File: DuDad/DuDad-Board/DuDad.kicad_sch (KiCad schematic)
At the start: 24 parts, among them J1 EXP, J2 USB_B_Micro, J3 USB_A, Q1 2N3906, Q2 2N3906, Q3 2N7000, Q4 2N3906, SW1 Reset

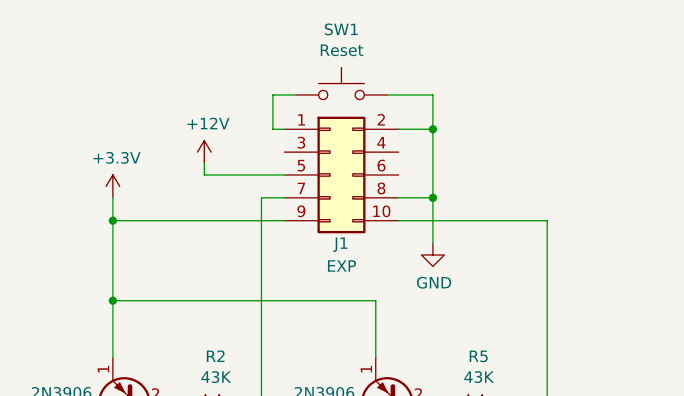
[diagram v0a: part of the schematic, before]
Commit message: Updates readme and DuDad board.
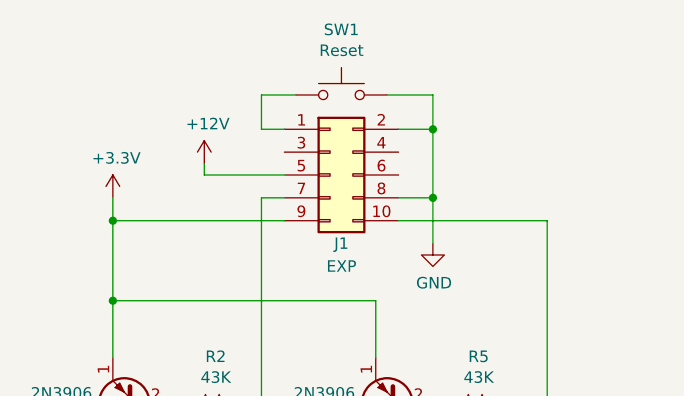
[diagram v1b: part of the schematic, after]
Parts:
- D1: Digi-Key Part 160-1035-ND -> 732-5005-ND
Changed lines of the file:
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@@
     (stroke (width 0) (type default) (color 0 0 0 0))
   )
-  (wire (pts (xy 49.53 33.02) (xy 49.53 29.21))
+  (wire (pts (xy 48.26 33.02) (xy 48.26 29.21))
     (stroke (width 0) (type default) (color 0 0 0 0))
   )
@@
     (stroke (width 0) (type default) (color 0 0 0 0))
   )
-  (wire (pts (xy 49.53 29.21) (xy 52.07 29.21))
+  (wire (pts (xy 48.26 29.21) (xy 52.07 29.21))
     (stroke (width 0) (type default) (color 0 0 0 0))
   )
@@
     (stroke (width 0) (type default) (color 0 0 0 0))
   )
-  (wire (pts (xy 50.8 33.02) (xy 49.53 33.02))
+  (wire (pts (xy 50.8 33.02) (xy 48.26 33.02))
     (stroke (width 0) (type default) (color 0 0 0 0))
   )
@@
       (effects (font (size 1.27 1.27)) hide)
     )
-    (property "Digi-Key Part" "160-1035-ND" (id 4) (at 31.75 73.66 90)
-      (effects (font (size 1.27 1.27)) hide)
-    )
+    (property "Digi-Key Part" "732-5005-ND" (id 4) (at 31.75 73.66 90)
+      (effects (font (size 1.27 1.27)) hide)
+    )

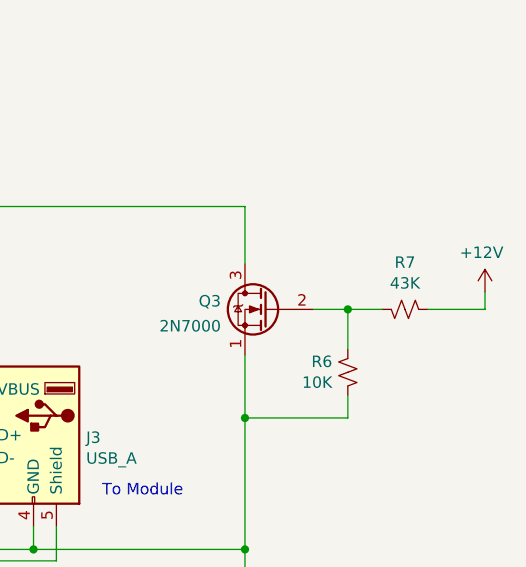
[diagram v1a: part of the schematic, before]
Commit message: Updates readme, moves docs to docs folder
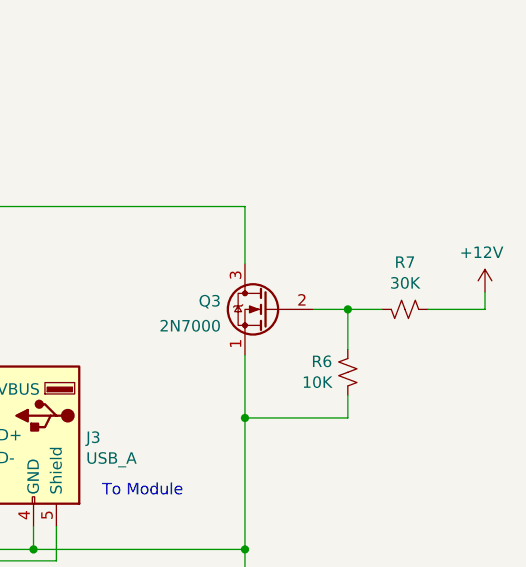
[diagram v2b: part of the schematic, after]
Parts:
- R7: value 43K -> 30K; Digi-Key Part CF14JT43K0CT-ND -> CF14JT30K0CT-ND
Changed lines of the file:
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@@
     (in_bom yes) (on_board yes)
     (property "Reference" "R7" (id 0) (at 187.96 69.088 90))
-    (property "Value" "43K" (id 1) (at 187.96 71.3994 90))
+    (property "Value" "30K" (id 1) (at 187.96 71.3994 90))
     (property "Footprint" "Resistor_THT:R_Axial_DIN0207_L6.3mm_D2.5mm_P10.16mm_Horizontal" (id 2) (at 187.96 74.295 0)
       (effects (font (size 1.27 1.27)) hide)
@@
       (effects (font (size 1.27 1.27)) hide)
     )
-    (property "Digi-Key Part" "CF14JT43K0CT-ND" (id 4) (at 187.96 74.295 90)
+    (property "Digi-Key Part" "CF14JT30K0CT-ND" (id 4) (at 187.96 74.295 90)
       (effects (font (size 1.27 1.27)) hide)
     )
@@
     )
     (path "/455ab60b-7725-47c1-8bea-8bb2de9c3df5"
-      (reference "R7") (unit 1) (value "43K") (footprint "Resistor_THT:R_Axial_DIN0207_L6.3mm_D2.5mm_P10.16mm_Horizontal")
+      (reference "R7") (unit 1) (value "30K") (footprint "Resistor_THT:R_Axial_DIN0207_L6.3mm_D2.5mm_P10.16mm_Horizontal")
     )
     (path "/cb20dedd-c678-4d7e-b310-0959ee8ccdca"

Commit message: Adds 2HP DuDad
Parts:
- J1:   LCSC Part # (none) -> C225520
- J3:   LCSC Part # (none) -> C718031
- Q1, Q2, Q4:   LCSC Part # (none) -> C9809
- Q3:   LCSC Part # (none) -> C232838
- R1, R4:   LCSC Part # (none) -> C119309
- R2, R5, R8:   LCSC Part # (none) -> C433719
- R3:   LCSC Part # (none) -> C410696
- R6, R9:   LCSC Part # (none) -> C433778
- R7:   LCSC Part # (none) -> C176499
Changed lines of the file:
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@@
+      (effects (font (size 1.27 1.27)) hide)
+    )
+    (property "  LCSC Part #" "C9809" (id 5) (at 63.5 63.5 0)
       (effects (font (size 1.27 1.27)) hide)
     )
@@
       (effects (font (size 1.27 1.27)) hide)
     )
+    (property "  LCSC Part #" "C433719" (id 5) (at 72.39 63.5 0)
+      (effects (font (size 1.27 1.27)) hide)
+    )
     (pin "1")
     (pin "2")
@@
     )
     (property "Digi-Key Part" "CF14JT200RCT-ND" (id 4) (at 60.96 81.28 0)
+      (effects (font (size 1.27 1.27)) hide)
+    )
+    (property "  LCSC Part #" "C119309" (id 5) (at 60.96 81.28 0)
       (effects (font (size 1.27 1.27)) hide)
     )
@@
       (effects (font (size 1.27 1.27)) hide)
     )
+    (property "  LCSC Part #" "C9809" (id 5) (at 34.29 63.5 0)
+      (effects (font (size 1.27 1.27)) hide)
+    )
     (pin "1")
     (pin "2")
@@
       (effects (font (size 1.27 1.27)) hide)
     )
+    (property "  LCSC Part #" "C433719" (id 5) (at 43.18 63.5 0)
+      (effects (font (size 1.27 1.27)) hide)
+    )
     (pin "1")
     (pin "2")
@@
     )
     (property "Digi-Key Part" "CF14JT200RCT-ND" (id 4) (at 31.75 81.28 0)
+      (effects (font (size 1.27 1.27)) hide)
+    )
+    (property "  LCSC Part #" "C119309" (id 5) (at 31.75 81.28 0)
       (effects (font (size 1.27 1.27)) hide)
     )
@@
     )
     (property "Digi-Key Part" "738-CFF14JT1K00CT-ND" (id 4) (at 133.985 120.015 0)
+      (effects (font (size 1.27 1.27)) hide)
+    )
+    (property "  LCSC Part #" "C410696" (id 5) (at 133.985 120.015 0)
       (effects (font (size 1.27 1.27)) hide)
     )
@@
       (effects (font (size 1.27 1.27)) hide)
     )
+    (property "  LCSC Part #" "C718031" (id 5) (at 146.685 88.265 0)
+      (effects (font (size 1.27 1.27)) hide)
+    )
     (pin "1")
     (pin "2")
@@
     )
     (property "Digi-Key Part" "S2011EC-05-ND" (id 4) (at 55.88 38.1 0)
+      (effects (font (size 1.27 1.27)) hide)
+    )
+    (property "  LCSC Part #" "C225520" (id 5) (at 55.88 38.1 0)
       (effects (font (size 1.27 1.27)) hide)
     )
@@
       (effects (font (size 1.27 1.27)) hide)
     )
+    (property "  LCSC Part #" "C9809" (id 5) (at 120.65 80.645 0)
+      (effects (font (size 1.27 1.27)) hide)
+    )
     (pin "1")
     (pin "2")
@@
       (effects (font (size 1.27 1.27)) hide)
     )
+    (property "  LCSC Part #" "C176499" (id 5) (at 187.96 74.295 90)
+      (effects (font (size 1.27 1.27)) hide)
+    )
     (pin "1")
     (pin "2")
@@
     )
     (property "Digi-Key Part" "CF14JT10K0CT-ND" (id 4) (at 131.445 62.865 0)
+      (effects (font (size 1.27 1.27)) hide)
+    )
+    (property "  LCSC Part #" "C433778" (id 5) (at 131.445 62.865 0)
       (effects (font (size 1.27 1.27)) hide)
     )
@@
       (effects (font (size 1.27 1.27)) hide)
     )
+    (property "  LCSC Part #" "C232838" (id 5) (at 172.72 74.295 0)
+      (effects (font (size 1.27 1.27)) hide)
+    )
     (pin "1")
     (pin "2")
@@
       (effects (font (size 1.27 1.27)) hide)
     )
+    (property "  LCSC Part #" "C433719" (id 5) (at 112.395 72.39 0)
+      (effects (font (size 1.27 1.27)) hide)
+    )
     (pin "1")
     (pin "2")
@@
       (effects (font (size 1.27 1.27)) hide)
     )
+    (property "  LCSC Part #" "C433778" (id 5) (at 181.61 81.28 0)
+      (effects (font (size 1.27 1.27)) hide)
+    )

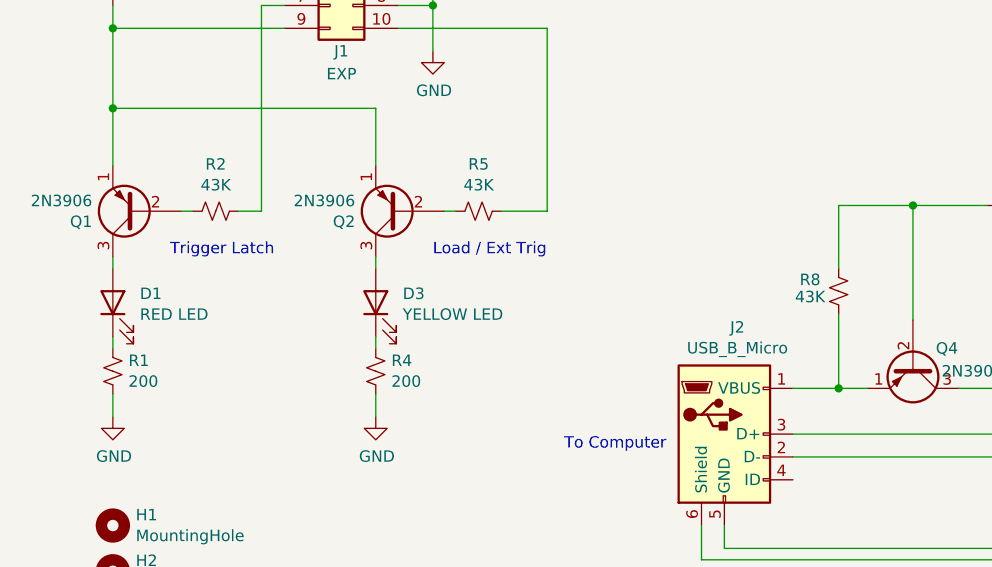
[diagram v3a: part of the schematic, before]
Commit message: Ups resistor values to dim LEDs. Adds generate BOMs.
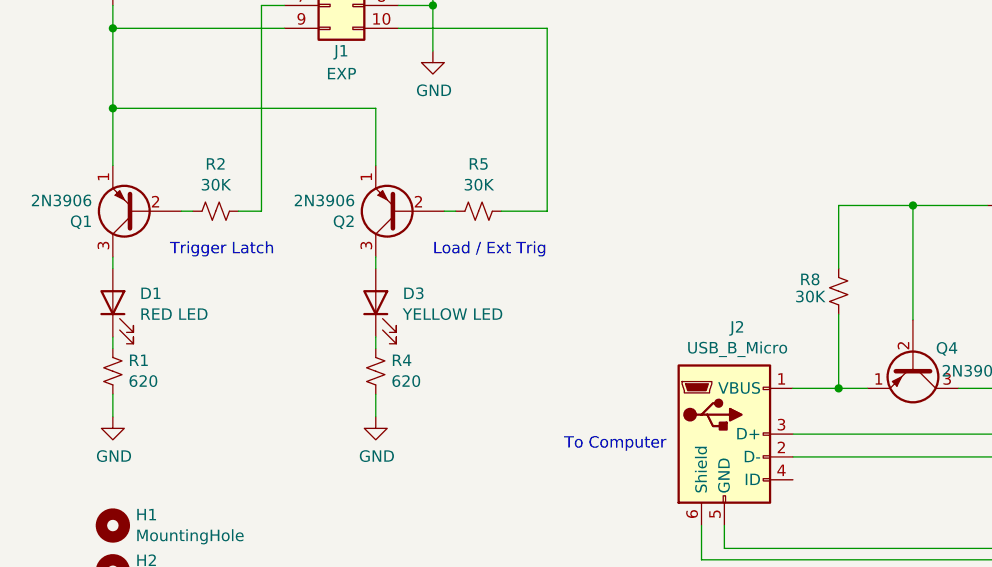
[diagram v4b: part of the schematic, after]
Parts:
- J1:   LCSC Part # C225520 -> (none); LCSC Part # (none) -> C225520
- J3:   LCSC Part # C718031 -> (none); LCSC Part # (none) -> C386737
- Q1, Q2, Q4:   LCSC Part # C9809 -> (none); LCSC Part # (none) -> C9809
- Q3:   LCSC Part # C232838 -> (none); LCSC Part # (none) -> C232838
- R1, R4: value 200 -> 620;   LCSC Part # C119309 -> (none); Digi-Key Part CF14JT200RCT-ND -> CF14JT620RCT-ND; LCSC Part # (none) -> C120050
- R2, R5, R8: value 43K -> 30K;   LCSC Part # C433719 -> (none); Digi-Key Part CF14JT43K0CT-ND -> CF14JT30K0CT-ND; LCSC Part # (none) -> C176499
- R3:   LCSC Part # C410696 -> (none); Digi-Key Part 738-CFF14JT1K00CT-ND -> CF14JT1K00CT-ND; LCSC Part # (none) -> C120055
- R6, R9:   LCSC Part # C433778 -> (none); LCSC Part # (none) -> C433778
- R7:   LCSC Part # C176499 -> (none); LCSC Part # (none) -> C176499
- SW1: Digi-Key Part 450-1940-ND -> 450-1653-ND
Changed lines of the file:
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@@
       (effects (font (size 1.27 1.27)) hide)
     )
-    (property "  LCSC Part #" "C9809" (id 5) (at 63.5 63.5 0)
+    (property "LCSC Part #" "C9809" (id 5) (at 63.5 63.5 0)
       (effects (font (size 1.27 1.27)) hide)
     )
@@
     (in_bom yes) (on_board yes)
     (property "Reference" "R5" (id 0) (at 72.39 58.293 90))
-    (property "Value" "43K" (id 1) (at 72.39 60.6044 90))
+    (property "Value" "30K" (id 1) (at 72.39 60.6044 90))
     (property "Footprint" "Resistor_THT:R_Axial_DIN0207_L6.3mm_D2.5mm_P10.16mm_Horizontal" (id 2) (at 72.39 63.5 0)
       (effects (font (size 1.27 1.27)) hide)
@@
       (effects (font (size 1.27 1.27)) hide)
     )
-    (property "Digi-Key Part" "CF14JT43K0CT-ND" (id 4) (at 72.39 63.5 90)
-      (effects (font (size 1.27 1.27)) hide)
-    )
-    (property "  LCSC Part #" "C433719" (id 5) (at 72.39 63.5 0)
+    (property "Digi-Key Part" "CF14JT30K0CT-ND" (id 4) (at 72.39 63.5 90)
+      (effects (font (size 1.27 1.27)) hide)
+    )
+    (property "LCSC Part #" "C176499" (id 5) (at 72.39 63.5 0)
       (effects (font (size 1.27 1.27)) hide)
     )
@@
       (effects (font (size 1.27 1.27)) (justify right))
     )
-    (property "Value" "200" (id 1) (at 62.6872 82.423 0)
+    (property "Value" "620" (id 1) (at 62.6872 82.423 0)
       (effects (font (size 1.27 1.27)) (justify right))
     )
@@
       (effects (font (size 1.27 1.27)) hide)
     )
-    (property "Digi-Key Part" "CF14JT200RCT-ND" (id 4) (at 60.96 81.28 0)
-      (effects (font (size 1.27 1.27)) hide)
-    )
-    (property "  LCSC Part #" "C119309" (id 5) (at 60.96 81.28 0)
+    (property "Digi-Key Part" "CF14JT620RCT-ND" (id 4) (at 60.96 81.28 0)
+      (effects (font (size 1.27 1.27)) hide)
+    )
+    (property "LCSC Part #" "C120050" (id 5) (at 60.96 81.28 0)
       (effects (font (size 1.27 1.27)) hide)
     )
@@
       (effects (font (size 1.27 1.27)) hide)
     )
-    (property "Digi-Key Part" "450-1940-ND" (id 4) (at 57.15 29.21 0)
+    (property "Digi-Key Part" "450-1653-ND" (id 4) (at 57.15 29.21 0)
       (effects (font (size 1.27 1.27)) hide)
     )
@@
       (effects (font (size 1.27 1.27)) hide)
     )
-    (property "  LCSC Part #" "C9809" (id 5) (at 34.29 63.5 0)
+    (property "LCSC Part #" "C9809" (id 5) (at 34.29 63.5 0)
       (effects (font (size 1.27 1.27)) hide)
     )
@@
     (in_bom yes) (on_board yes)
     (property "Reference" "R2" (id 0) (at 43.18 58.293 90))
-    (property "Value" "43K" (id 1) (at 43.18 60.6044 90))
+    (property "Value" "30K" (id 1) (at 43.18 60.6044 90))
     (property "Footprint" "Resistor_THT:R_Axial_DIN0207_L6.3mm_D2.5mm_P10.16mm_Horizontal" (id 2) (at 43.18 63.5 0)
       (effects (font (size 1.27 1.27)) hide)
@@
       (effects (font (size 1.27 1.27)) hide)
     )
-    (property "Digi-Key Part" "CF14JT43K0CT-ND" (id 4) (at 43.18 63.5 90)
-      (effects (font (size 1.27 1.27)) hide)
-    )
-    (property "  LCSC Part #" "C433719" (id 5) (at 43.18 63.5 0)
+    (property "Digi-Key Part" "CF14JT30K0CT-ND" (id 4) (at 43.18 63.5 90)
+      (effects (font (size 1.27 1.27)) hide)
+    )
+    (property "LCSC Part #" "C176499" (id 5) (at 43.18 63.5 0)
       (effects (font (size 1.27 1.27)) hide)
     )
@@
       (effects (font (size 1.27 1.27)) (justify right))
     )
-    (property "Value" "200" (id 1) (at 33.4772 82.423 0)
+    (property "Value" "620" (id 1) (at 33.4772 82.423 0)
       (effects (font (size 1.27 1.27)) (justify right))
     )
@@
       (effects (font (size 1.27 1.27)) hide)
     )
-    (property "Digi-Key Part" "CF14JT200RCT-ND" (id 4) (at 31.75 81.28 0)
-      (effects (font (size 1.27 1.27)) hide)
-    )
-    (property "  LCSC Part #" "C119309" (id 5) (at 31.75 81.28 0)
+    (property "Digi-Key Part" "CF14JT620RCT-ND" (id 4) (at 31.75 81.28 0)
+      (effects (font (size 1.27 1.27)) hide)
+    )
+    (property "LCSC Part #" "C120050" (id 5) (at 31.75 81.28 0)
       (effects (font (size 1.27 1.27)) hide)
     )
@@
       (effects (font (size 1.27 1.27)) hide)
     )
-    (property "Digi-Key Part" "738-CFF14JT1K00CT-ND" (id 4) (at 133.985 120.015 0)
-      (effects (font (size 1.27 1.27)) hide)
-    )
-    (property "  LCSC Part #" "C410696" (id 5) (at 133.985 120.015 0)
+    (property "Digi-Key Part" "CF14JT1K00CT-ND" (id 4) (at 133.985 120.015 0)
+      (effects (font (size 1.27 1.27)) hide)
+    )
+    (property "LCSC Part #" "C120055" (id 5) (at 133.985 120.015 0)
       (effects (font (size 1.27 1.27)) hide)
     )
@@
       (effects (font (size 1.27 1.27)) hide)
     )
-    (property "  LCSC Part #" "C718031" (id 5) (at 146.685 88.265 0)
+    (property "LCSC Part #" "C386737" (id 5) (at 146.685 88.265 0)
       (effects (font (size 1.27 1.27)) hide)
     )
@@
       (effects (font (size 1.27 1.27)) hide)
     )
-    (property "  LCSC Part #" "C225520" (id 5) (at 55.88 38.1 0)
+    (property "LCSC Part #" "C225520" (id 5) (at 55.88 38.1 0)
       (effects (font (size 1.27 1.27)) hide)
     )
@@
       (effects (font (size 1.27 1.27)) hide)
     )
-    (property "  LCSC Part #" "C9809" (id 5) (at 120.65 80.645 0)
+    (property "LCSC Part #" "C9809" (id 5) (at 120.65 80.645 0)
       (effects (font (size 1.27 1.27)) hide)
     )
@@
       (effects (font (size 1.27 1.27)) hide)
     )
-    (property "  LCSC Part #" "C176499" (id 5) (at 187.96 74.295 90)
+    (property "LCSC Part #" "C176499" (id 5) (at 187.96 74.295 90)
       (effects (font (size 1.27 1.27)) hide)
     )
@@
       (effects (font (size 1.27 1.27)) hide)
     )
-    (property "  LCSC Part #" "C433778" (id 5) (at 131.445 62.865 0)
+    (property "LCSC Part #" "C433778" (id 5) (at 131.445 62.865 0)
       (effects (font (size 1.27 1.27)) hide)
     )
@@
       (effects (font (size 1.27 1.27)) hide)
     )
-    (property "  LCSC Part #" "C232838" (id 5) (at 172.72 74.295 0)
+    (property "LCSC Part #" "C232838" (id 5) (at 172.72 74.295 0)
       (effects (font (size 1.27 1.27)) hide)
     )
@@
     (in_bom yes) (on_board yes)
     (property "Reference" "R8" (id 0) (at 109.22 71.12 0))
-    (property "Value" "43K" (id 1) (at 109.22 73.025 0))
+    (property "Value" "30K" (id 1) (at 109.22 73.025 0))
     (property "Footprint" "Resistor_THT:R_Axial_DIN0207_L6.3mm_D2.5mm_P10.16mm_Horizontal" (id 2) (at 112.395 72.39 0)
       (effects (font (size 1.27 1.27)) hide)
@@
       (effects (font (size 1.27 1.27)) hide)
     )
-    (property "Digi-Key Part" "CF14JT43K0CT-ND" (id 4) (at 112.395 72.39 90)
-      (effects (font (size 1.27 1.27)) hide)
-    )
-    (property "  LCSC Part #" "C433719" (id 5) (at 112.395 72.39 0)
+    (property "Digi-Key Part" "CF14JT30K0CT-ND" (id 4) (at 112.395 72.39 90)
+      (effects (font (size 1.27 1.27)) hide)
+    )
+    (property "LCSC Part #" "C176499" (id 5) (at 112.395 72.39 0)
       (effects (font (size 1.27 1.27)) hide)
     )
@@
       (effects (font (size 1.27 1.27)) hide)
     )
-    (property "  LCSC Part #" "C433778" (id 5) (at 181.61 81.28 0)
+    (property "LCSC Part #" "C433778" (id 5) (at 181.61 81.28 0)
       (effects (font (size 1.27 1.27)) hide)
     )
@@
     )
     (path "/00000000-0000-0000-0000-0000620129e0"
-      (reference "R1") (unit 1) (value "200") (footprint "Resistor_THT:R_Axial_DIN0207_L6.3mm_D2.5mm_P10.16mm_Horizontal")
+      (reference "R1") (unit 1) (value "620") (footprint "Resistor_THT:R_Axial_DIN0207_L6.3mm_D2.5mm_P10.16mm_Horizontal")
     )
     (path "/00000000-0000-0000-0000-000062010975"
-      (reference "R2") (unit 1) (value "43K") (footprint "Resistor_THT:R_Axial_DIN0207_L6.3mm_D2.5mm_P10.16mm_Horizontal")
+      (reference "R2") (unit 1) (value "30K") (footprint "Resistor_THT:R_Axial_DIN0207_L6.3mm_D2.5mm_P10.16mm_Horizontal")
     )
     (path "/00000000-0000-0000-0000-0000620806b7"
@@
     )
     (path "/00000000-0000-0000-0000-000061f47872"
-      (reference "R4") (unit 1) (value "200") (footprint "Resistor_THT:R_Axial_DIN0207_L6.3mm_D2.5mm_P10.16mm_Horizontal")
+      (reference "R4") (unit 1) (value "620") (footprint "Resistor_THT:R_Axial_DIN0207_L6.3mm_D2.5mm_P10.16mm_Horizontal")
     )
     (path "/00000000-0000-0000-0000-000061f47868"
-      (reference "R5") (unit 1) (value "43K") (footprint "Resistor_THT:R_Axial_DIN0207_L6.3mm_D2.5mm_P10.16mm_Horizontal")
+      (reference "R5") (unit 1) (value "30K") (footprint "Resistor_THT:R_Axial_DIN0207_L6.3mm_D2.5mm_P10.16mm_Horizontal")
     )
     (path "/d2010513-d039-43c6-bd57-c1f921d695f9"
@@
     )
     (path "/cb20dedd-c678-4d7e-b310-0959ee8ccdca"
-      (reference "R8") (unit 1) (value "43K") (footprint "Resistor_THT:R_Axial_DIN0207_L6.3mm_D2.5mm_P10.16mm_Horizontal")
+      (reference "R8") (unit 1) (value "30K") (footprint "Resistor_THT:R_Axial_DIN0207_L6.3mm_D2.5mm_P10.16mm_Horizontal")
     )
     (path "/73c4cd56-fccd-4694-b5c7-de65ffb51867"
